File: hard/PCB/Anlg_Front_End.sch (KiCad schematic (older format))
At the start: 1 part

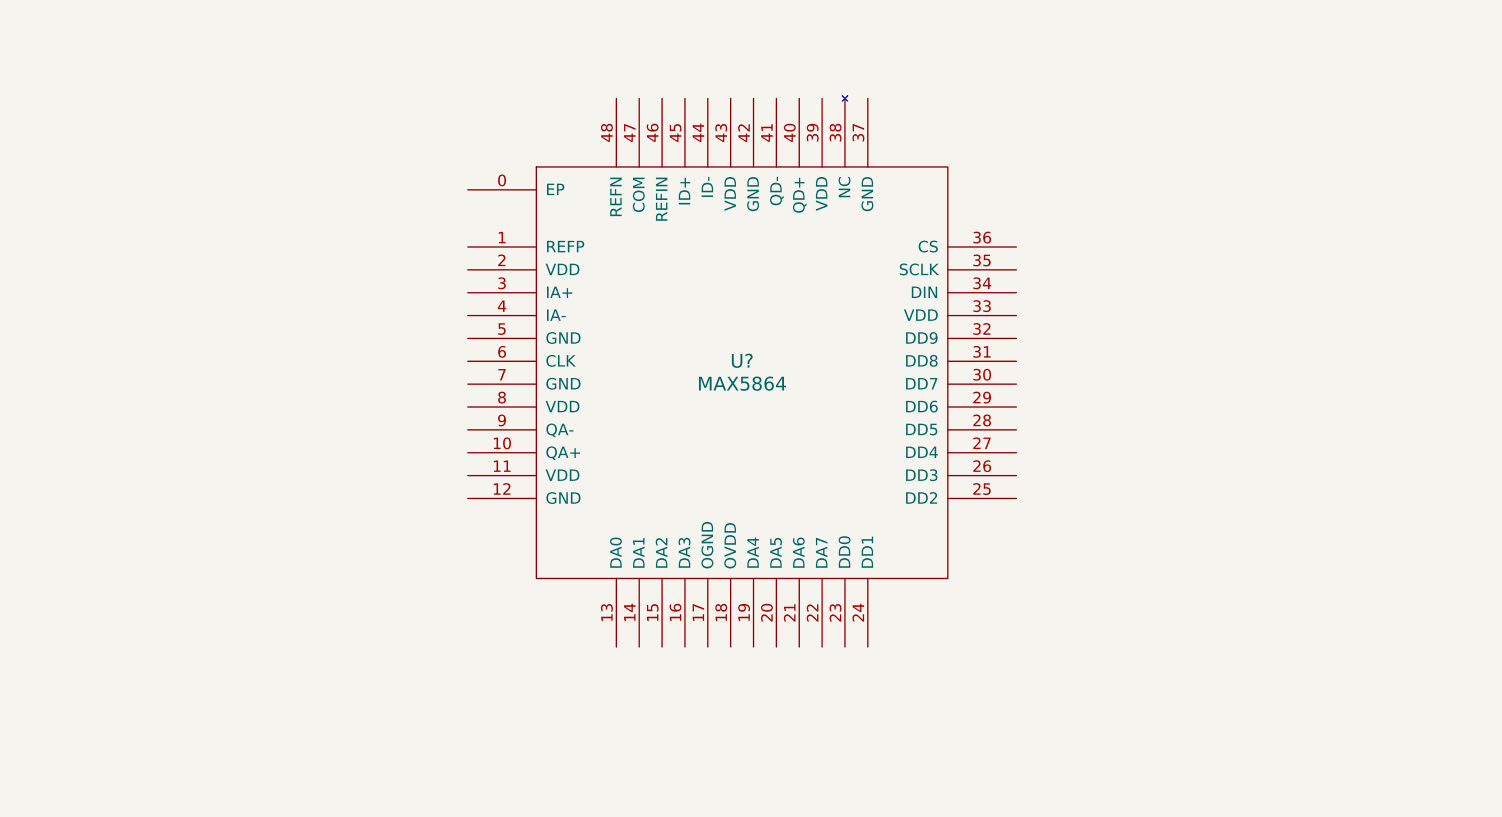
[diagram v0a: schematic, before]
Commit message: Update supply power
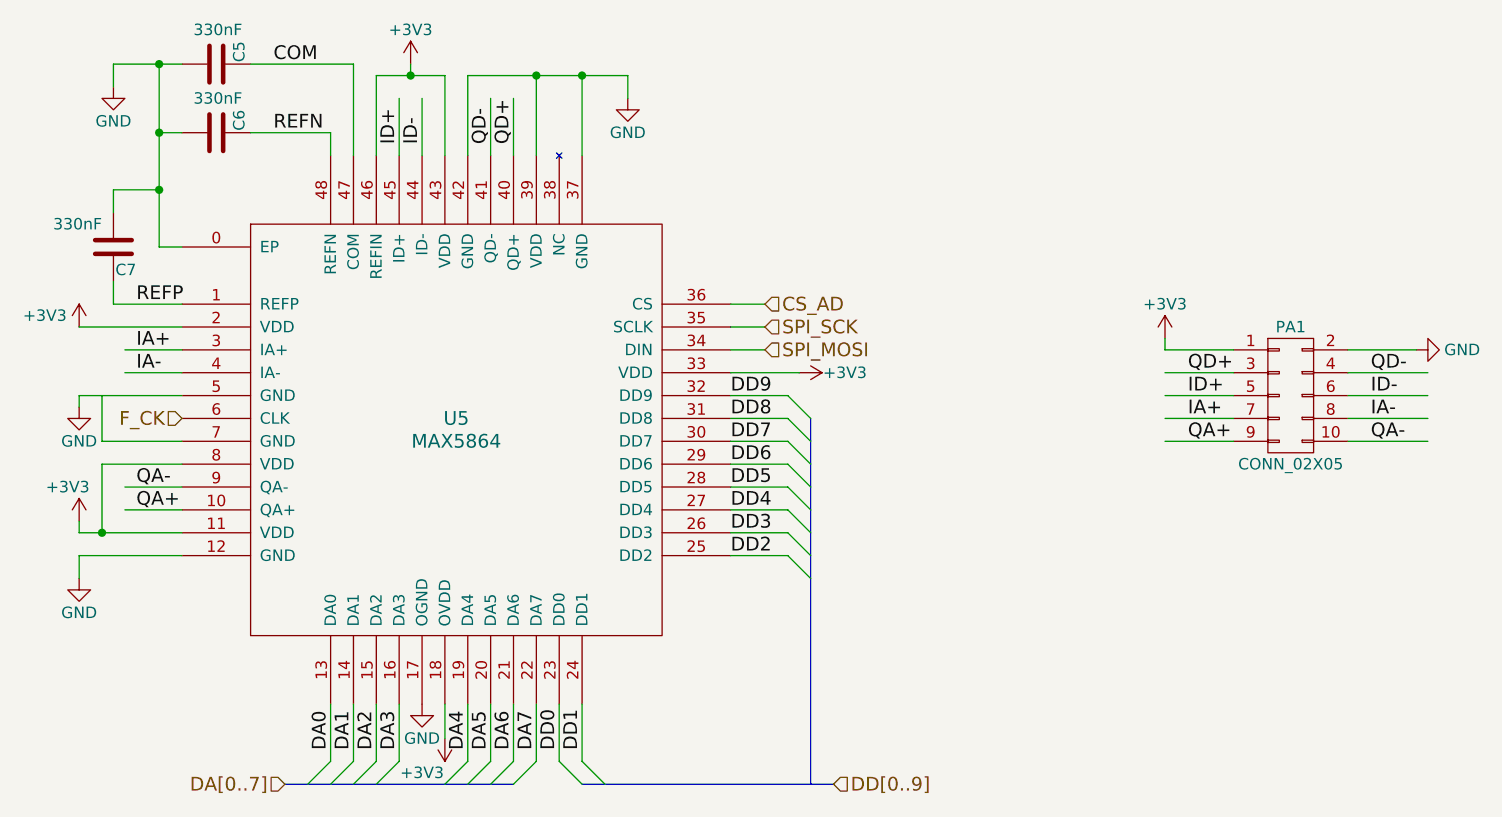
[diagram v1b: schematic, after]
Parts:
- added C5, C6, C7: 330nF, Capacitors_SMD:C_0402, symbol C
- added PA1: CONN_02X05, Pin_Headers:Pin_Header_Straight_2x05_Pitch2.54mm, symbol CONN_02X05
- U5: renamed from U?; footprint (none) -> Project:GSG-QFN48-7; DIGIKEY REF (none) -> MAX5864ETM+-ND
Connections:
- net labels added: +3V3, COM, CS_AD, DA0, DA1, DA2, DA3, DA4, DA5, DA6, DA7, DA[0..7], DD0, DD1, DD2, DD3, DD4, DD5, DD6, DD7, DD8, DD9, DD[0..9], F_CK, GND, IA+, IA-, ID+, ID-, QA+, QA-, QD+, QD-, REFN, REFP, SPI_MOSI, SPI_SCK
- wire segments 0 -> 75
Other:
- moved on the sheet: U5
